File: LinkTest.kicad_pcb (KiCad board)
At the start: 4 copper layers, 62 x 70 mm, 80 parts, among them J1 Amphenol_901-144, J2 Conn_01x04_Socket, J3 Amphenol_901-144, Q1 IRLML2803, Q2 IRLML2803, U1 RFM98PW, U2 TPS54426PWPR, U3 LORA1280F27-TCXO, U4 ADM1176-1ARMZ-R7

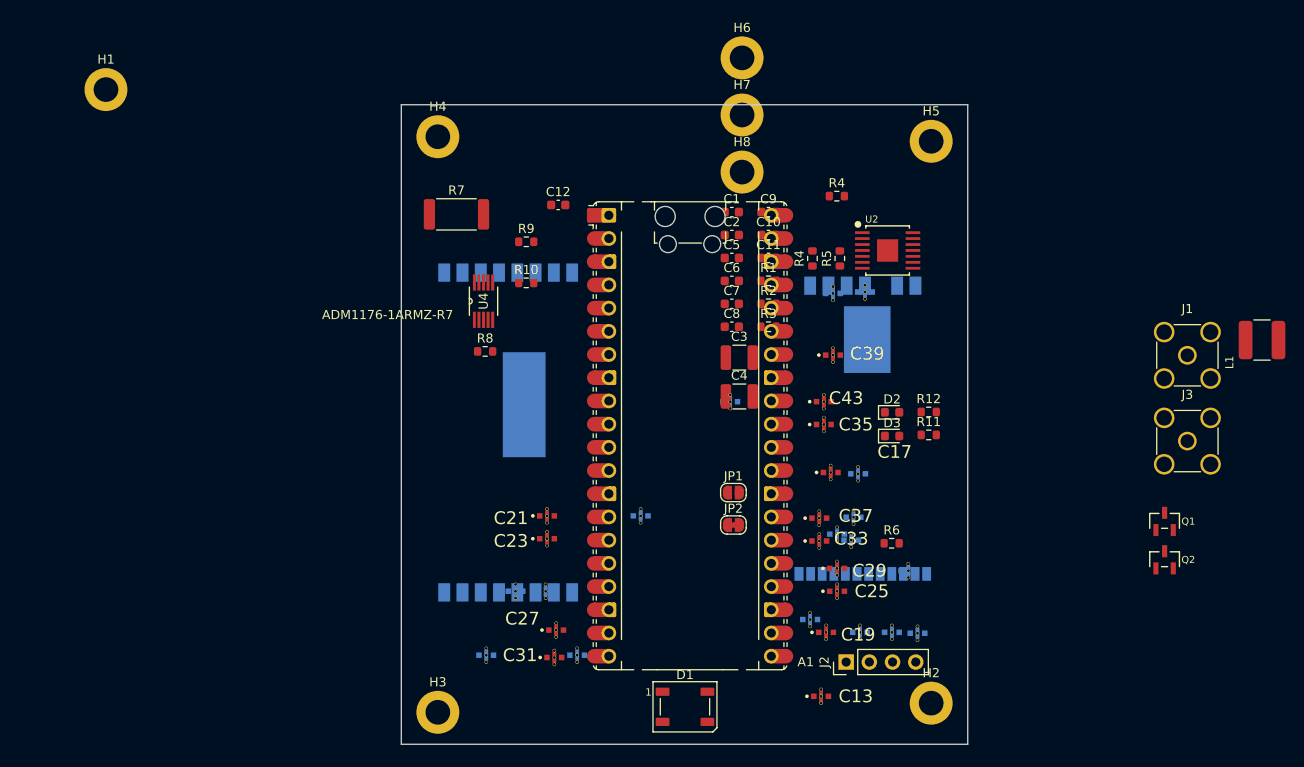
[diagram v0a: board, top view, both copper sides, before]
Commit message: Feedthrough symbol and footprint
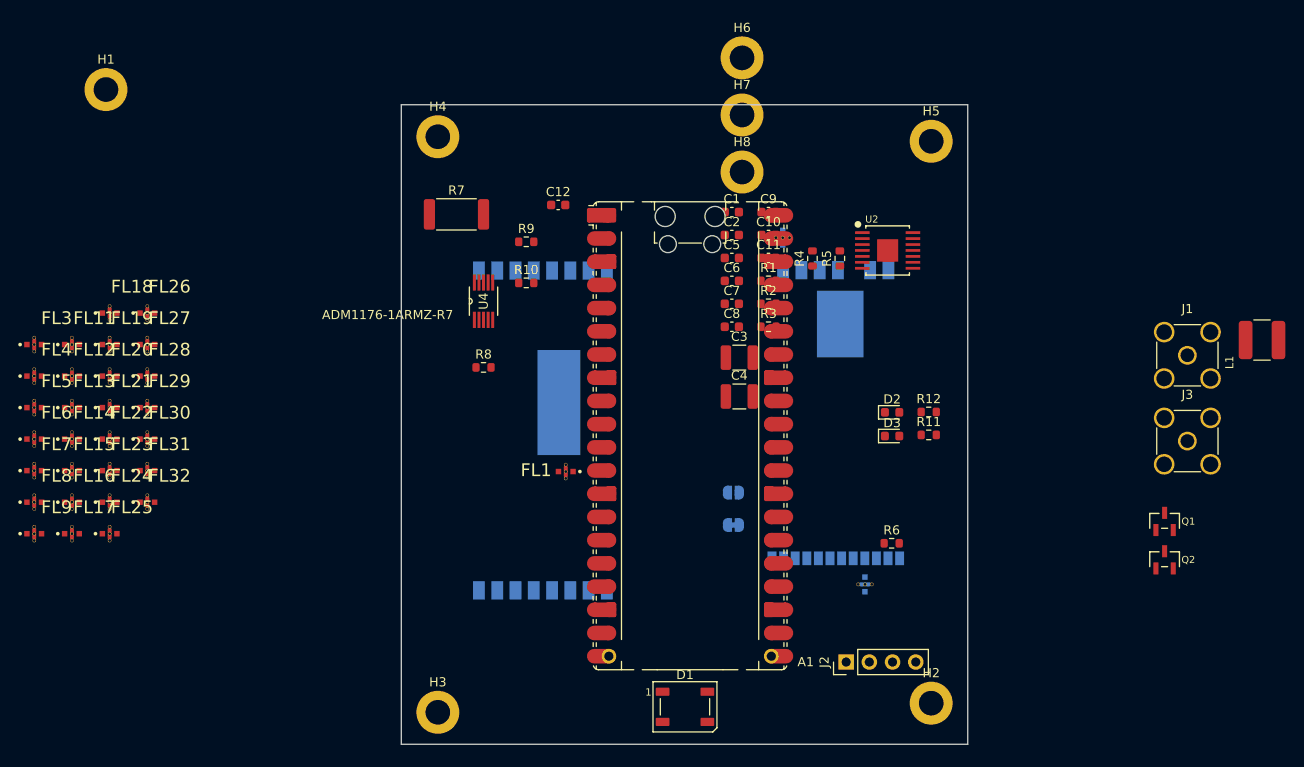
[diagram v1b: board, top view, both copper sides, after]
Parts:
- removed C13, C14, C16, C17, C18, C19, C20, C21, C22, C23, C24, C25, C26, C27, C28, C29, C30, C31, C32, C33, C34, C35, C36, C37, C38, C39, C40, C41, C42, C43, C44: 100 p, NFM18CC101R1C3D:FIL_NFM18CC101R1C3D
- removed the R4 at (169.7, 73.5)
- added FL1: NFM18CC101R1C3D, NFM18CC101R1C3D:FIL_NFM18CC101R1C3D, F.Cu at (140.0, 103.7)
- added FL10: NFM18CC101R1C3D, NFM18CC101R1C3D:FIL_NFM18CC101R1C3D, B.Cu at (172.8, 116.0)
- added FL11: NFM18CC101R1C3D, NFM18CC101R1C3D:FIL_NFM18CC101R1C3D, F.Cu at (86.0, 89.8)
- added FL12: NFM18CC101R1C3D, NFM18CC101R1C3D:FIL_NFM18CC101R1C3D, F.Cu at (86.0, 93.2)
- added FL13: NFM18CC101R1C3D, NFM18CC101R1C3D:FIL_NFM18CC101R1C3D, F.Cu at (86.0, 96.7)
- added FL14: NFM18CC101R1C3D, NFM18CC101R1C3D:FIL_NFM18CC101R1C3D, F.Cu at (86.0, 100.1)
- added FL15: NFM18CC101R1C3D, NFM18CC101R1C3D:FIL_NFM18CC101R1C3D, F.Cu at (86.0, 103.5)
- added FL16: NFM18CC101R1C3D, NFM18CC101R1C3D:FIL_NFM18CC101R1C3D, F.Cu at (86.0, 107.0)
- added FL17: NFM18CC101R1C3D, NFM18CC101R1C3D:FIL_NFM18CC101R1C3D, F.Cu at (86.0, 110.5)
- added FL18: NFM18CC101R1C3D, NFM18CC101R1C3D:FIL_NFM18CC101R1C3D, F.Cu at (90.1, 86.3)
- added FL19: NFM18CC101R1C3D, NFM18CC101R1C3D:FIL_NFM18CC101R1C3D, F.Cu at (90.1, 89.8)
- added FL2: NFM18CC101R1C3D, NFM18CC101R1C3D:FIL_NFM18CC101R1C3D, B.Cu at (163.8, 78.0)
- added FL20: NFM18CC101R1C3D, NFM18CC101R1C3D:FIL_NFM18CC101R1C3D, F.Cu at (90.1, 93.2)
- added FL21: NFM18CC101R1C3D, NFM18CC101R1C3D:FIL_NFM18CC101R1C3D, F.Cu at (90.1, 96.7)
- added FL22: NFM18CC101R1C3D, NFM18CC101R1C3D:FIL_NFM18CC101R1C3D, F.Cu at (90.1, 100.1)
- added FL23: NFM18CC101R1C3D, NFM18CC101R1C3D:FIL_NFM18CC101R1C3D, F.Cu at (90.1, 103.5)
- added FL24: NFM18CC101R1C3D, NFM18CC101R1C3D:FIL_NFM18CC101R1C3D, F.Cu at (90.1, 107.0)
- added FL25: NFM18CC101R1C3D, NFM18CC101R1C3D:FIL_NFM18CC101R1C3D, F.Cu at (90.1, 110.5)
- added FL26: NFM18CC101R1C3D, NFM18CC101R1C3D:FIL_NFM18CC101R1C3D, F.Cu at (94.2, 86.3)
- added FL27: NFM18CC101R1C3D, NFM18CC101R1C3D:FIL_NFM18CC101R1C3D, F.Cu at (94.2, 89.8)
- added FL28: NFM18CC101R1C3D, NFM18CC101R1C3D:FIL_NFM18CC101R1C3D, F.Cu at (94.2, 93.2)
- added FL29: NFM18CC101R1C3D, NFM18CC101R1C3D:FIL_NFM18CC101R1C3D, F.Cu at (94.2, 96.7)
- added FL3: NFM18CC101R1C3D, NFM18CC101R1C3D:FIL_NFM18CC101R1C3D, F.Cu at (81.8, 89.8)
- added FL30: NFM18CC101R1C3D, NFM18CC101R1C3D:FIL_NFM18CC101R1C3D, F.Cu at (94.2, 100.1)
- added FL31: NFM18CC101R1C3D, NFM18CC101R1C3D:FIL_NFM18CC101R1C3D, F.Cu at (94.2, 103.5)
- added FL32: NFM18CC101R1C3D, NFM18CC101R1C3D:FIL_NFM18CC101R1C3D, F.Cu at (94.2, 107.0)
- added FL4: NFM18CC101R1C3D, NFM18CC101R1C3D:FIL_NFM18CC101R1C3D, F.Cu at (81.8, 93.2)
- added FL5: NFM18CC101R1C3D, NFM18CC101R1C3D:FIL_NFM18CC101R1C3D, F.Cu at (81.8, 96.7)
- added FL6: NFM18CC101R1C3D, NFM18CC101R1C3D:FIL_NFM18CC101R1C3D, F.Cu at (81.8, 100.1)
- added FL7: NFM18CC101R1C3D, NFM18CC101R1C3D:FIL_NFM18CC101R1C3D, F.Cu at (81.8, 103.5)
- added FL8: NFM18CC101R1C3D, NFM18CC101R1C3D:FIL_NFM18CC101R1C3D, F.Cu at (81.8, 107.0)
- added FL9: NFM18CC101R1C3D, NFM18CC101R1C3D:FIL_NFM18CC101R1C3D, F.Cu at (81.8, 110.5)
- JP1, JP2: moved to B.Cu
- moved U1 3.81 mm to (137.5, 99.2)
- moved U3 3.41 mm to (161.7, 81.6)
- moved R8 1.76 mm to (131.0, 92.2)

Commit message: started placement of feed through
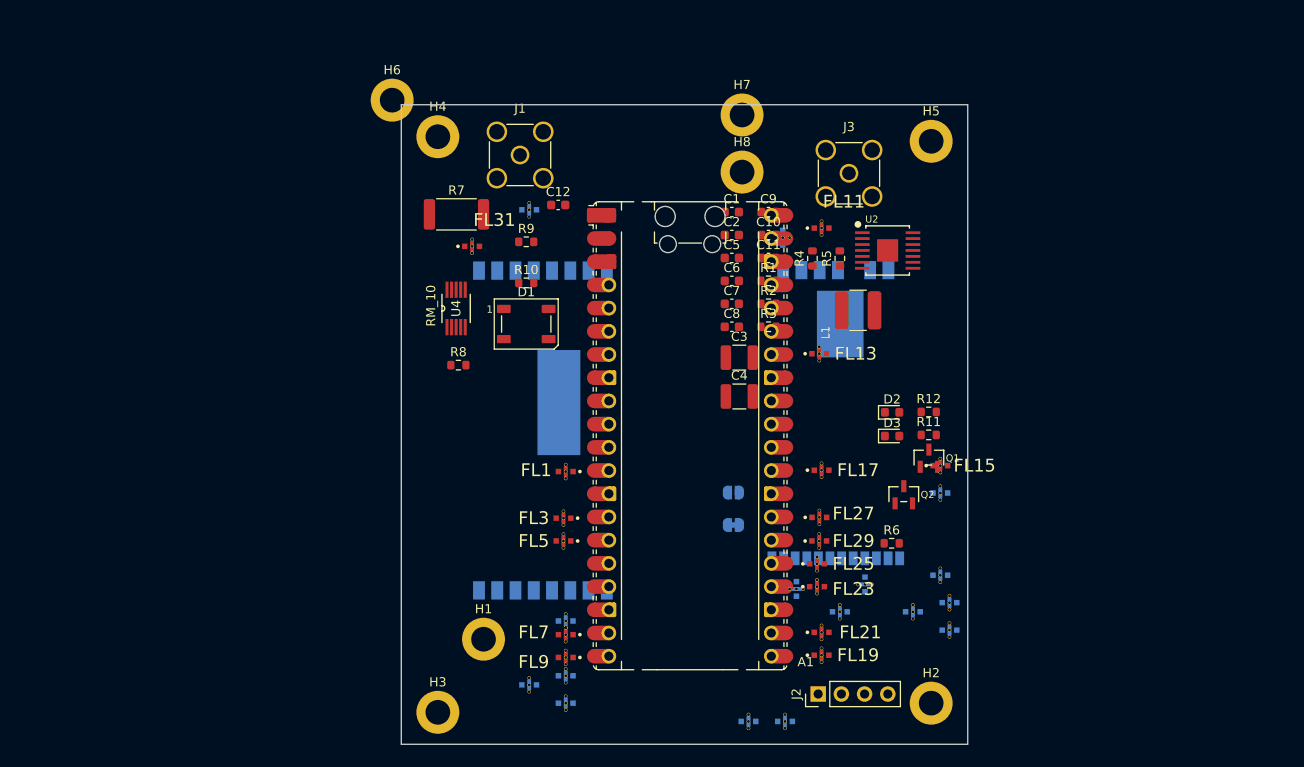
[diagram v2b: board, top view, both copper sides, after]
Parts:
- FL12, FL14, FL16, FL18, FL20, FL22, FL24, FL26, FL28, FL30, FL32, FL4, FL6, FL8: moved to B.Cu
- U4: value ADM1176-1ARMZ-R7 -> RM_10
- moved FL4 99.6 mm to (178.0, 119.0)
- moved FL18 97.2 mm to (182.0, 118.0)
- moved FL16 95.4 mm to (181.0, 115.0)
- moved FL15 95.1 mm to (181.0, 103.0)
- moved FL24 93.0 mm to (182.0, 121.0)
- moved FL28 87.7 mm to (181.0, 106.0)
- moved FL14 86.1 mm to (170.0, 119.0)
- moved FL8 85.6 mm to (164.0, 131.0)
- moved FL19 85.0 mm to (168.0, 123.8)
- moved FL6 84.1 mm to (160.0, 131.0)
- moved FL11 83.0 mm to (168.0, 77.0)
- moved FL12 82.7 mm to (165.2, 116.5), turned to 90 degrees
- moved FL17 82.3 mm to (168.0, 103.5)
- moved FL13 82.0 mm to (167.8, 90.8)
- moved FL21 81.7 mm to (168.0, 121.2)
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
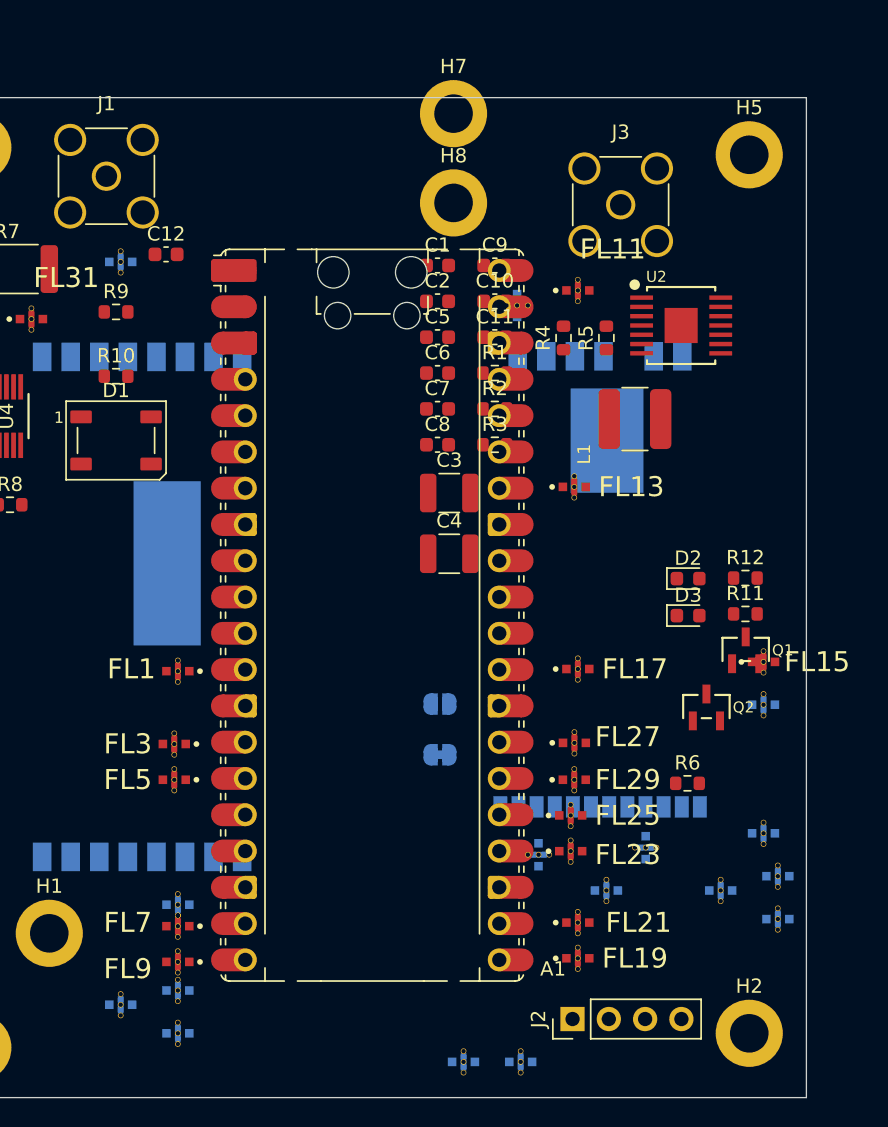
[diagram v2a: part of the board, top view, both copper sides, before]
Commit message: SMD Pads on pico
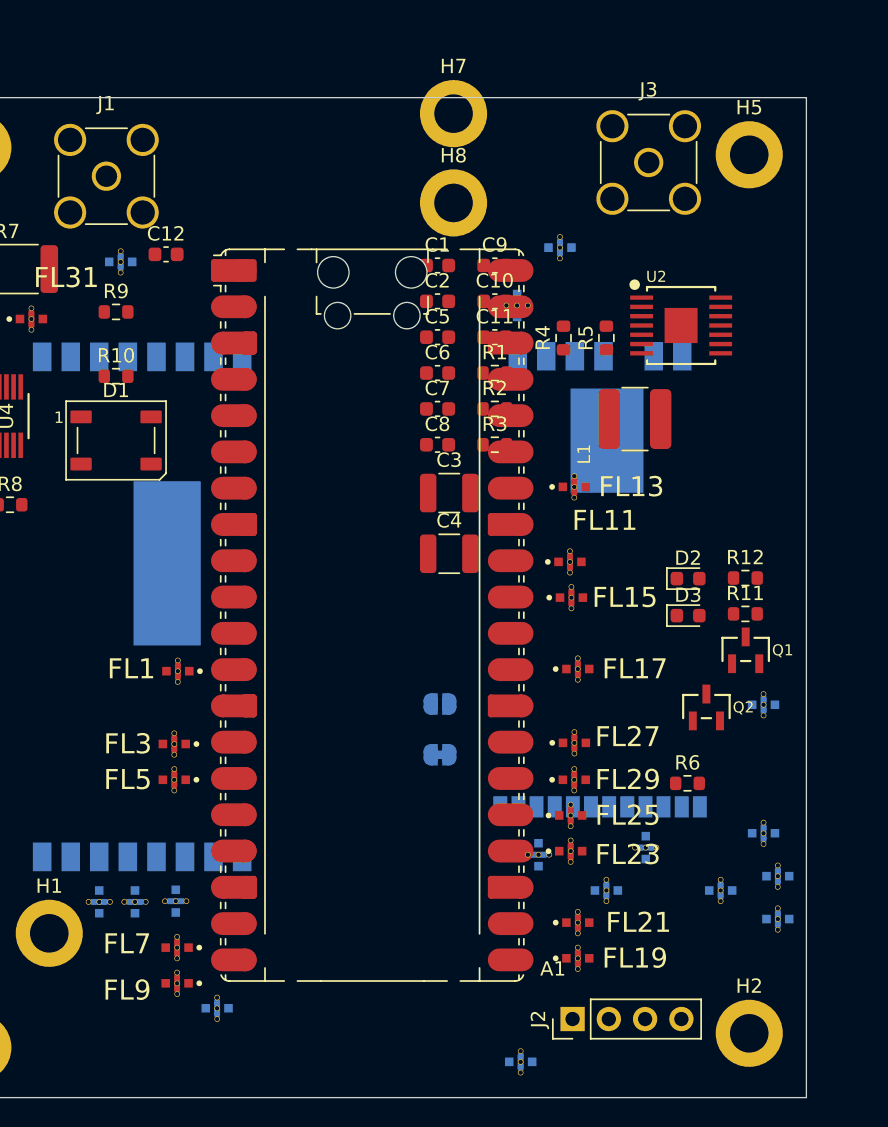
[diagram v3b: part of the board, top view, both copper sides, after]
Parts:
- moved FL6 57.4 mm to (166.8, 74.0)
- moved FL11 19.0 mm to (167.4, 96.0)
- moved FL15 14.2 mm to (167.6, 98.5)
- moved FL22 9.68 mm to (137.0, 119.8), turned to 90 degrees
- moved FL20 7.75 mm to (142.8, 127.2), turned to 180 degrees
- moved FL30 7.35 mm to (134.5, 119.8), turned to 90 degrees
- moved FL26 6.25 mm to (139.8, 119.8), turned to 90 degrees
- moved J3 3.55 mm to (173.0, 68.0)
- moved FL7 1.50 mm to (139.9, 123.0)
- moved FL9 1.50 mm to (139.9, 125.5)

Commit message: remove CS pullup
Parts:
- removed R1: 10k, Resistor_SMD:R_0603_1608Metric
- U4: value RM_10 -> ADM1176-1ARMZ-R7
- moved FL28 49.0 mm to (140.5, 78.5), turned to -90 degrees
- moved FL24 44.8 mm to (137.2, 123.5), turned to 90 degrees
- moved H7 40.5 mm to (180.8, 99.0)
- moved H6 33.7 mm to (125.2, 96.5)
- moved FL16 15.6 mm to (165.5, 116.3), turned to 90 degrees
- moved FL18 11.4 mm to (170.7, 116.2), turned to 90 degrees
- moved FL8 10.6 mm to (165.8, 120.5), turned to 90 degrees
- moved FL14 9.89 mm to (160.5, 116.3), turned to 90 degrees
- moved FL20 7.45 mm to (142.8, 119.8), turned to 90 degrees
- moved H8 7.11 mm to (153.5, 66.8)
- moved FL6 4.03 mm to (166.2, 78.0), turned to -90 degrees
- moved FL4 3.62 mm to (175.7, 116.2), turned to 90 degrees
- moved FL32 3.47 mm to (133.0, 76.8), turned to 90 degrees
- moved FL12 2.27 mm to (163.0, 116.3)
- moved FL25 1.52 mm to (167.8, 115.2)
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
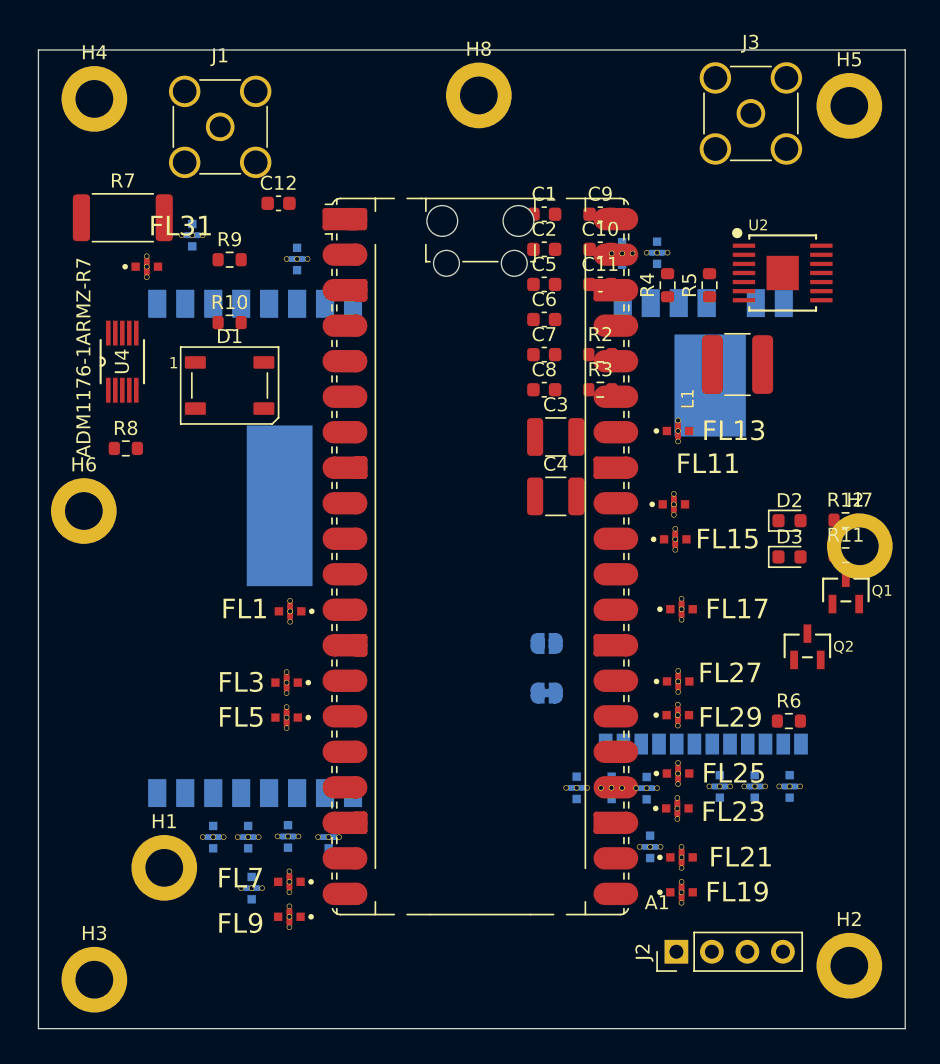
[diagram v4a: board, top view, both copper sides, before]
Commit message: Antenna connection, gnd planes, in process of getting feedthrough caps to connect to ground
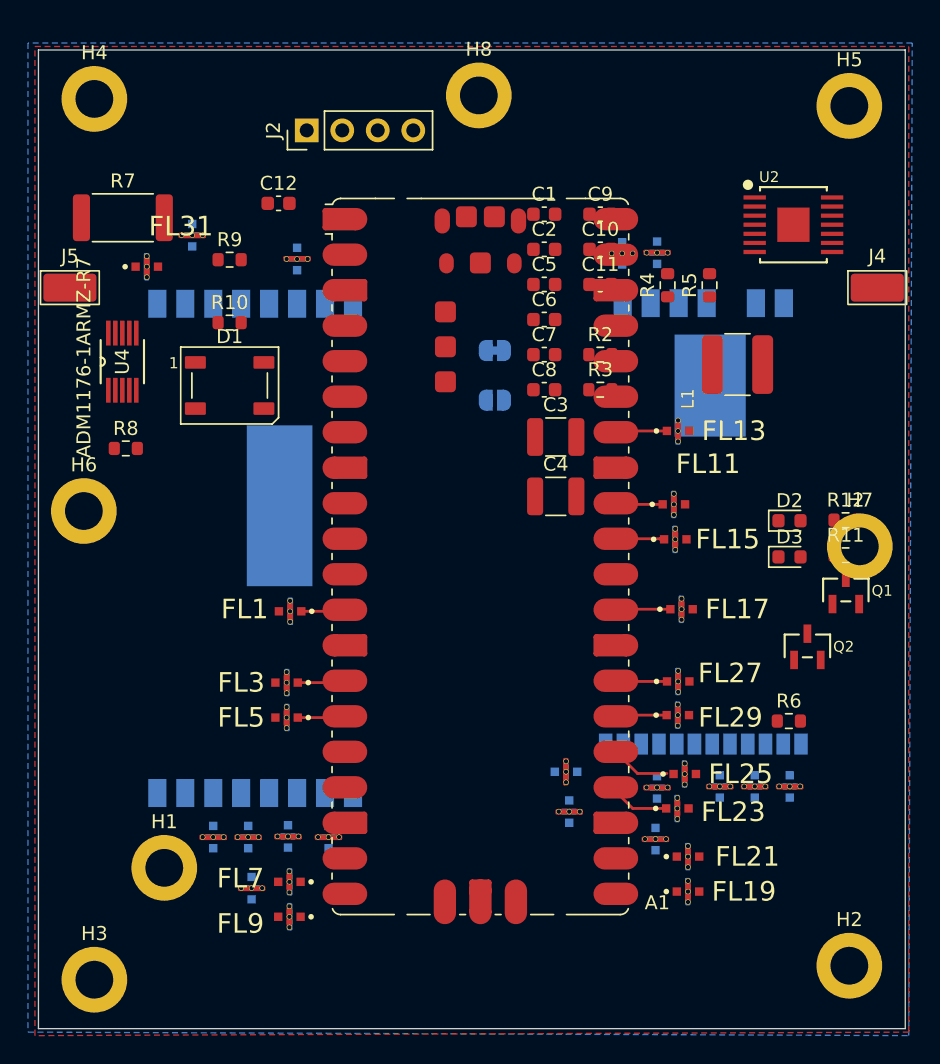
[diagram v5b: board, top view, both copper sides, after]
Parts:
- removed J1, J3: Amphenol_901-144, ssi_connector:SMA_Amphenol_901-144_horizontal
- added J4: Conn_01x01, TestPoint:TestPoint_Keystone_5019_Miniature, F.Cu at (182.0, 80.5)
- added J5: Conn_01x01, TestPoint:TestPoint_Keystone_5019_Miniature, F.Cu at (124.2, 80.5)
- A1: footprint Module:RaspberryPi_Pico_Common_Unspecified -> Module:RaspberryPi_Pico_SMD
- moved J2 64.4 mm to (141.2, 69.2)
- moved JP2 24.8 mm to (154.7, 85.0), turned to 180 degrees
- moved JP1 17.8 mm to (154.7, 88.5), turned to 180 degrees
- moved U2 3.53 mm to (176.0, 76.0)
- moved FL12 3.47 mm to (160.0, 118.0)
- moved FL14 1.38 mm to (159.7, 115.1), turned to 0 degrees
- moved FL16 0.75 mm to (166.2, 116.2)
- moved FL8 0.68 mm to (166.1, 119.9)
- moved FL25 0.48 mm to (168.2, 115.3)
- moved FL19 0.46 mm to (168.5, 123.7)
- moved FL21 0.46 mm to (168.5, 121.2)
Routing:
- net UHF_MOSI_C: track 0.00 -> 4.29 mm
- net UHF_SCK_C: track 0.00 -> 4.01 mm
- net SBAND_D1_C: track 0.00 -> 3.92 mm
- net SBAND_MISO_C: track 0.00 -> 3.69 mm
- net UHF_RST_C: track 0.00 -> 3.68 mm
- net UHF_D0_C: track 0.00 -> 3.67 mm
- net SBAND_SCK_C: track 0.00 -> 3.47 mm
- net SBAND_RST_C: track 0.00 -> 3.42 mm
- net SBAND_RXEN_C: track 0.00 -> 3.41 mm
- net SBAND_MOSI_C: track 0.00 -> 3.38 mm
- net SBAND_TXEN_C: track 0.00 -> 3.17 mm
- added copper zone on B.Cu, net GND
- added copper zone on F.Cu, net GND
- added copper zone on In1.Cu, net GND
- removed copper zone on In1.Cu, net 5V
